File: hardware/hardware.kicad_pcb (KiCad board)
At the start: 4 copper layers, 102 parts, among them IC1 TAS5760LDAPR, J1 798-DM3D-SF, J2 Conn_01x04, J3 Conn_01x04, J4 USB-C, SW1 SW_Push, SW2 SW_Push, SW3 SW_Push, SW5 SW_Push, U1 TPS563200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

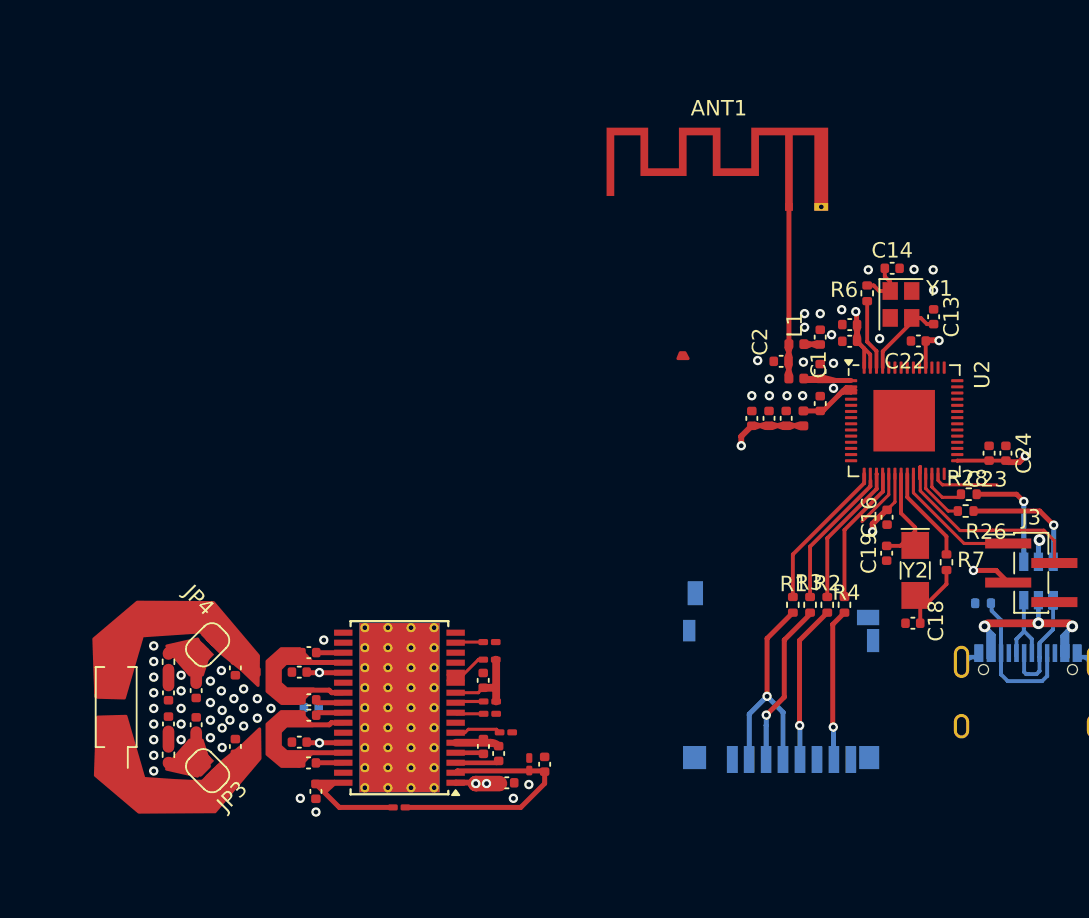
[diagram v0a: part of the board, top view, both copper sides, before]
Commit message: realocando estruturas
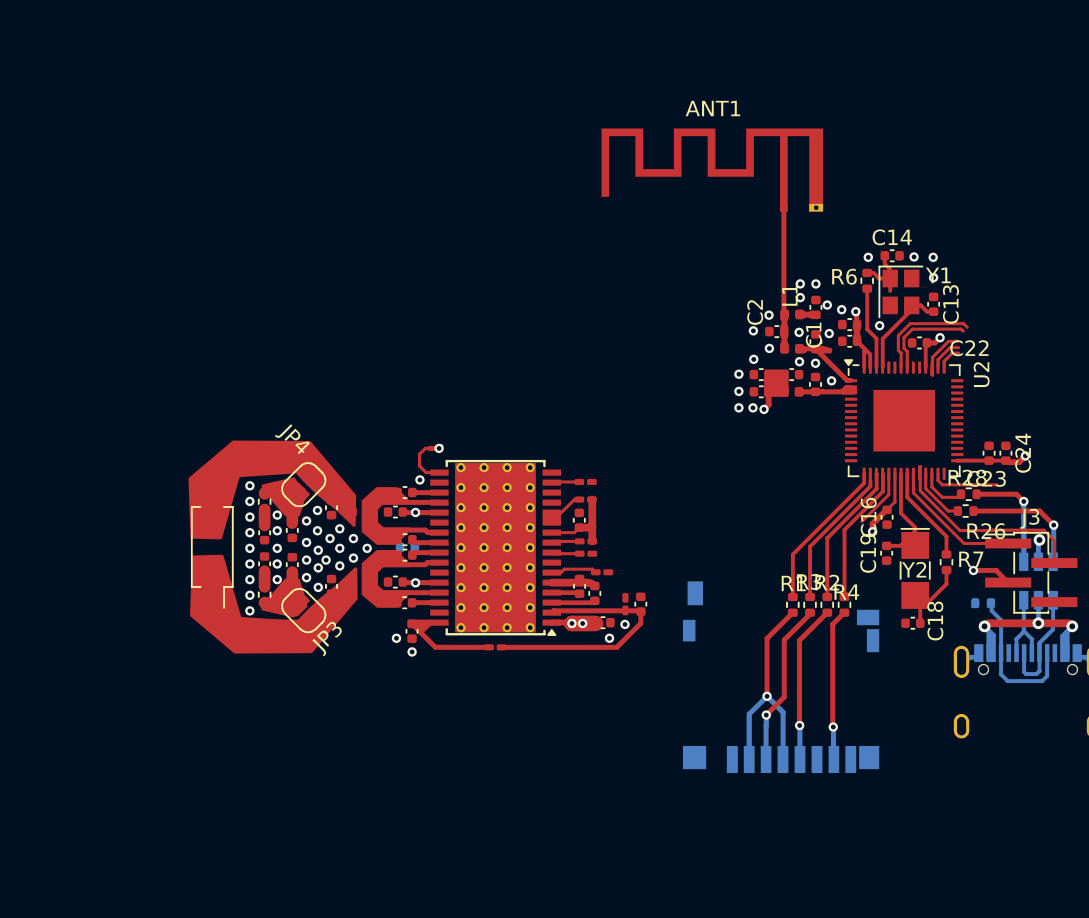
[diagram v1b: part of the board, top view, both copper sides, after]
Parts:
- moved C43 12.1 mm to (97.5, 97.9)
- moved L5 12.1 mm to (103.7, 99.1)
- moved C44 12.1 mm to (97.5, 95.9)
- moved R24 12.1 mm to (97.5, 93.9)
- moved C32 12.1 mm to (106.6, 93.3)
- moved C36 12.1 mm to (101.8, 94.3)
- moved C42 12.1 mm to (119.5, 101.7)
- moved C31 12.1 mm to (106.6, 100.5)
- moved L6 12.1 mm to (103.7, 94.5)
- moved LS1 12.1 mm to (94.1, 96.8)
- moved R14 12.1 mm to (118.4, 97.3)
- moved R15 12.1 mm to (118.4, 92.6)
- moved C25 12.1 mm to (118.0, 95.1)
- moved C26 12.1 mm to (119.0, 99.8)
- moved C27 12.1 mm to (118.0, 99.4)
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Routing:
- net RX0: track 0.00 -> 7.05 mm
- net Net-(U2-U0TXD): track 0.00 -> 6.18 mm
- net LRCK: track 0.00 -> 3.84 mm, vias 0 -> 1
- net LED_B: track 0.00 -> 3.71 mm
- net LED_G: track 0.00 -> 2.18 mm
- net Net-(ANT1-Pad1): track 11.2 -> 9.26 mm
- net LED_R: track 0.00 -> 1.57 mm
- net 3V3: track 41.5 -> 40.2 mm
- net Net-(U2-XTAL_N): track 5.31 -> 6.13 mm
- net Net-(U2-XTAL_P): track 4.57 -> 5.38 mm
- net Net-(C9-Pad2): track 5.92 -> 5.26 mm
- net GND: vias 56 -> 60

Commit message: footprint socket 01x04 atualizado - partiu casa
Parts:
- D1, J2, J3: footprint Connector_PinHeader_1.27mm:PinHeader_1x04_P1.27mm_Vertical_SMD_Pin1Left -> Connector_PinSocket_1.27mm:PinSocket_1x04_P1.27mm_Vertical_SMD_Pin1Left
- moved D1 56.6 mm to (160.5, 92.8), turned to 180 degrees
- moved R19 55.0 mm to (157.2, 85.7), turned to -90 degrees
- moved J2 50.9 mm to (147.5, 80.2)
- moved R8 50.3 mm to (142.9, 82.7), turned to 180 degrees
- moved R18 45.5 mm to (157.3, 80.4)
- moved R17 45.5 mm to (157.3, 78.4)
- moved C42 4.77 mm to (120.0, 97.0)
- moved C25 4.77 mm to (118.5, 90.3)
- moved C26 4.77 mm to (119.5, 95.1)
- moved C30 4.77 mm to (107.6, 97.6)
- moved C31 4.77 mm to (107.1, 95.7)
- moved C32 4.77 mm to (107.1, 88.5)
- moved C33 4.77 mm to (107.1, 92.6)
- moved C35 4.77 mm to (102.4, 94.6)
- moved C36 4.77 mm to (102.4, 89.5)
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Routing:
- net RX0: track 7.05 -> 14.0 mm
- net TX0: track 0.00 -> 3.45 mm
- net 3V3: track 40.2 -> 43.3 mm, vias 6 -> 7
- net Net-(U2-U0TXD): track 6.18 -> 5.58 mm

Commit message: antes da aula
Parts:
- moved R10 150.5 mm to (169.5, 62.7), turned to -90 degrees
- moved R9 149.4 mm to (171.7, 62.6), turned to 90 degrees
- moved R5 146.3 mm to (167.6, 65.2), turned to 180 degrees
- moved C11 143.4 mm to (160.0, 65.9), turned to -90 degrees
- moved C15 143.1 mm to (166.0, 61.6), turned to 180 degrees
- moved U1 141.3 mm to (164.4, 65.2)
- moved C8 132.4 mm to (158.0, 65.8), turned to -90 degrees
- moved C20 128.9 mm to (150.6, 56.6)
- moved C21 128.9 mm to (150.6, 59.1)
- moved L4 128.9 mm to (144.6, 56.6)
- moved C17 128.9 mm to (150.6, 54.1)
- moved C6 128.5 mm to (155.5, 65.8), turned to -90 degrees
- moved SW5 115.9 mm to (115.6, 98.7), turned to 180 degrees
- moved SW3 115.9 mm to (115.6, 93.9), turned to 180 degrees
- moved R21 114.9 mm to (120.6, 93.4), turned to -90 degrees
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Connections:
- C13 pad 1: GND -> GPIO_45_46
- C14 pad 2: GND -> GPIO_45_46
- C18 pad 2: GND -> GPIO_45_46
- C19 pad 1: GND -> GPIO_45_46
- C25 pad 2: GND -> GPIO_45_46
- C30 pad 1: GND -> GPIO_45_46
- C35 pad 1: GND -> GPIO_45_46
- C36 pad 2: GND -> GPIO_45_46
- C37 pad 1: GND -> GPIO_45_46
- C38 pad 1: GND -> GPIO_45_46
- C39 pad 1: GND -> GPIO_45_46
- C40 pad 1: GND -> GPIO_45_46
- C41 pad 2: GND -> GPIO_45_46
- C42 pad 1: GND -> GPIO_45_46
- C43 pad 1: GND -> GPIO_45_46
- C44 pad 2: GND -> GPIO_45_46
- C46 pad 2: GND -> GPIO_45_46
- IC1 pad 18: GND -> GPIO_45_46
- IC1 pad 22: GND -> GPIO_45_46
- IC1 pad 27: GND -> GPIO_45_46
- IC1 pad 31: GND -> GPIO_45_46
- IC1 pad 33: GND -> GPIO_45_46
- J4 pad A1: GND -> GPIO_45_46
- J4 pad A12: GND -> GPIO_45_46
- J4 pad B1: GND -> GPIO_45_46
- J4 pad B12: GND -> GPIO_45_46
- J4 pad S1: GND -> GPIO_45_46
- R22 pad 2: GND -> GPIO_45_46
- R29 pad 2: GND -> GPIO_45_46
- U3 pad 2: GND -> GPIO_45_46
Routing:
- net GPIO_45_46: track 0.00 -> 14.6 mm, vias 0 -> 61
- net 12: track 0.00 -> 13.7 mm, vias 0 -> 2
- net Net-(U1-SW): track 0.00 -> 11.6 mm, vias 0 -> 5
- net Net-(U1-VFB): track 0.00 -> 9.63 mm
- net LED_R: track 1.57 -> 6.96 mm
- net Net-(D1-GK): track 0.00 -> 4.83 mm
- net LED_G: track 2.18 -> 6.56 mm
- net I2C_CLK: track 0.00 -> 4.35 mm, vias 0 -> 1
- net AUDIO_CLK: track 0.00 -> 4.34 mm, vias 0 -> 1
- net GND: track 4.15 -> 0.00 mm, vias 60 -> 0
- net Net-(U1-VBST): track 0.00 -> 3.85 mm
- net AUDIO_MUTE: track 0.00 -> 3.73 mm, vias 0 -> 1
- net LED_B: track 3.71 -> 7.29 mm
- net I2C_DATA_IN: track 0.00 -> 3.28 mm, vias 0 -> 1
- net JTAG: track 0.00 -> 2.49 mm
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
